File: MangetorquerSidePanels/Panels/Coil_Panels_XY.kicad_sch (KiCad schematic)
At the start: 9 parts, among them J1 Through_Hole_1, J2 MOLEX_2053380006

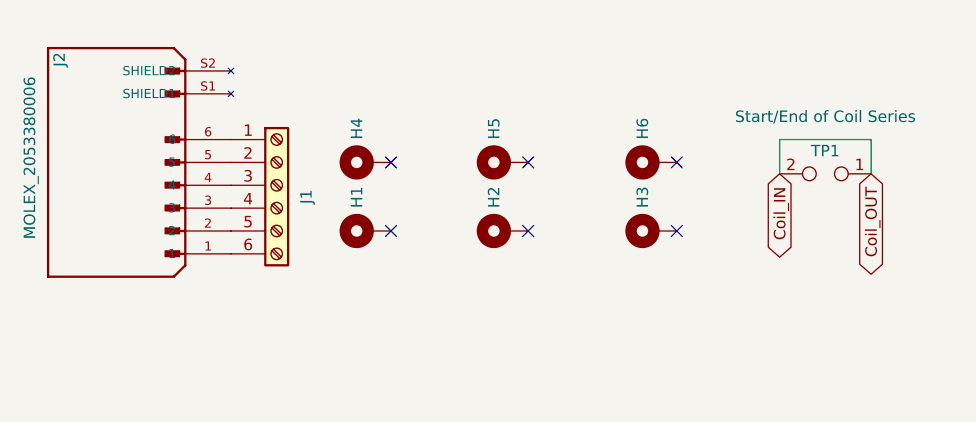
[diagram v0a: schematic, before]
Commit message: Final flight side panels w/ magnetorquers finished, note final board thickness of 0.031'' and updated copper weight of 0.5oz for internal layers
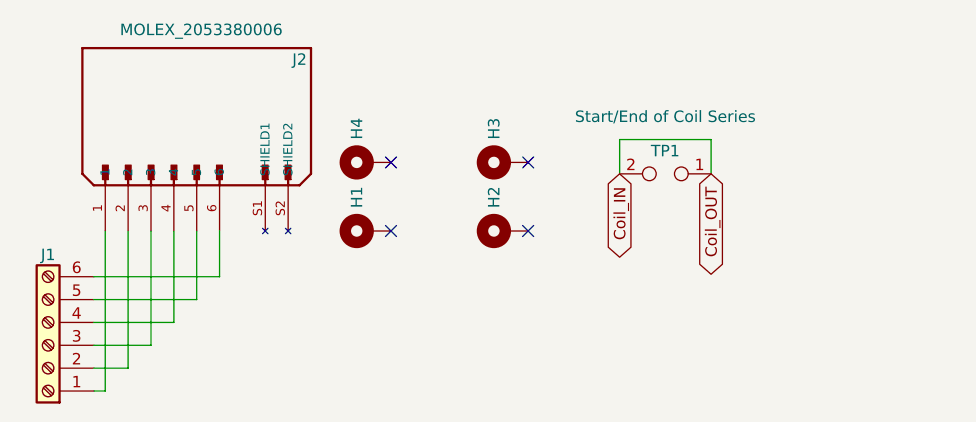
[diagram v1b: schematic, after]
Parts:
- removed H5, H6: ~, MountingHole:MountingHole_2.2mm_M2_DIN965_Pad_TopBottom, symbol Mechanical:MountingHole_Pad
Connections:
- net at J2.1: now also J1.1 (Pin_1); no longer J1.6 (Pin_6)
- net at J2.2: now also J1.2 (Pin_2); no longer J1.5 (Pin_5)
- net at J2.3: now also J1.3 (Pin_3); no longer J1.4 (Pin_4)
- net at J2.4: now also J1.4 (Pin_4); no longer J1.3 (Pin_3)
- net at J2.5: now also J1.5 (Pin_5); no longer J1.2 (Pin_2)
- net at J2.6: now also J1.6 (Pin_6); no longer J1.1 (Pin_1)
- no-connect marks 6 -> 4
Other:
- moved on the sheet: H3, J1, J2, TP1
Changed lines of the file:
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@@
 (kicad_sch (version 20211123) (generator eeschema)
   (paper "A4")
-  (no_connect (at 153.67 92.71))
   (no_connect (at 153.67 100.33))
   (no_connect (at 138.43 92.71))
   (no_connect (at 138.43 100.33))
-  (no_connect (at 170.18 92.71))
-  (no_connect (at 170.18 100.33))
-  (wire (pts (xy 191.77 93.98) (xy 191.77 90.17))
+  (no_connect (at 153.67 92.71))
+  (wire (pts (xy 106.68 118.11) (xy 106.68 100.33))
     (stroke (width 0) (type default) (color 0 0 0 0))
   )
-  (wire (pts (xy 191.77 90.17) (xy 181.61 90.17))
+  (wire (pts (xy 105.41 118.11) (xy 106.68 118.11))
     (stroke (width 0) (type default) (color 0 0 0 0))
   )
-  (wire (pts (xy 181.61 90.17) (xy 181.61 93.98))
+  (wire (pts (xy 105.41 115.57) (xy 109.22 115.57))
     (stroke (width 0) (type default) (color 0 0 0 0))
   )
-  (global_label "Coil_OUT" (shape bidirectional) (at 191.77 93.98 270) (fields_autoplaced)
+  (wire (pts (xy 105.41 107.95) (xy 116.84 107.95))
+    (stroke (width 0) (type default) (color 0 0 0 0))
+  )
+  (wire (pts (xy 116.84 107.95) (xy 116.84 100.33))
+    (stroke (width 0) (type default) (color 0 0 0 0))
+  )
+  (wire (pts (xy 105.41 110.49) (xy 114.3 110.49))
+    (stroke (width 0) (type default) (color 0 0 0 0))
+  )
+  (wire (pts (xy 111.76 113.03) (xy 111.76 100.33))
+    (stroke (width 0) (type default) (color 0 0 0 0))
+  )
+  (wire (pts (xy 109.22 115.57) (xy 109.22 100.33))
+    (stroke (width 0) (type default) (color 0 0 0 0))
+  )
+  (wire (pts (xy 105.41 105.41) (xy 119.38 105.41))
+    (stroke (width 0) (type default) (color 0 0 0 0))
+  )
+  (wire (pts (xy 173.99 93.98) (xy 173.99 90.17))
+    (stroke (width 0) (type default) (color 0 0 0 0))
+  )
+  (wire (pts (xy 114.3 110.49) (xy 114.3 100.33))
+    (stroke (width 0) (type default) (color 0 0 0 0))
+  )
+  (wire (pts (xy 119.38 105.41) (xy 119.38 100.33))
+    (stroke (width 0) (type default) (color 0 0 0 0))
+  )
+  (wire (pts (xy 173.99 90.17) (xy 163.83 90.17))
+    (stroke (width 0) (type default) (color 0 0 0 0))
+  )
+  (wire (pts (xy 163.83 90.17) (xy 163.83 93.98))
+    (stroke (width 0) (type default) (color 0 0 0 0))
+  )
+  (wire (pts (xy 105.41 113.03) (xy 111.76 113.03))
+    (stroke (width 0) (type default) (color 0 0 0 0))
+  )
+  (global_label "Coil_OUT" (shape bidirectional) (at 173.99 93.98 270) (fields_autoplaced)
     (effects (font (size 1.27 1.27)) (justify right))
-    (property "Intersheet References" "${INTERSHEET_REFS}" (id 0) (at 191.8494 104.6783 90)
+    (property "Intersheet References" "${INTERSHEET_REFS}" (id 0) (at 174.0694 104.6783 90)
       (effects (font (size 1.27 1.27)) (justify right) hide)
     )
   )
-  (global_label "Coil_IN" (shape bidirectional) (at 181.61 93.98 270) (fields_autoplaced)
+  (global_label "Coil_IN" (shape bidirectional) (at 163.83 93.98 270) (fields_autoplaced)
     (effects (font (size 1.27 1.27)) (justify right))
-    (property "Intersheet References" "${INTERSHEET_REFS}" (id 0) (at 181.6894 102.985 90)
+    (property "Intersheet References" "${INTERSHEET_REFS}" (id 0) (at 163.9094 102.985 90)
       (effects (font (size 1.27 1.27)) (justify right) hide)
     )
@@
     (pin "1")
   )
-  (symbol (lib_id "solar-panel-side-X-plus-rescue:2053380006-sapling") (at 107.95 92.71 180) (unit 1)
+  (symbol (lib_id "solar-panel-side-X-plus-rescue:2053380006-sapling") (at 116.84 87.63 90) (unit 1)
     (in_bom yes) (on_board yes)
-    (property "Reference" "J2" (id 0) (at 101.6 81.28 90))
-    (property "Value" "MOLEX_2053380006" (id 1) (at 98.298 92.202 90))
-    (property "Footprint" "panels:MOLEX_2053380006" (id 2) (at 107.95 92.71 0)
+    (property "Reference" "J2" (id 0) (at 128.27 81.28 90))
+    (property "Value" "MOLEX_2053380006" (id 1) (at 117.348 77.978 90))
+    (property "Footprint" "panels:MOLEX_2053380006" (id 2) (at 116.84 87.63 0)
       (effects (font (size 1.27 1.27)) hide)
     )
-    (property "Datasheet" "https://www.molex.com/webdocs/datasheets/pdf/en-us/2053380006_PCB_HEADERS.pdf" (id 3) (at 107.95 92.71 0)
+    (property "Datasheet" "https://www.molex.com/webdocs/datasheets/pdf/en-us/2053380006_PCB_HEADERS.pdf" (id 3) (at 116.84 87.63 0)
       (effects (font (size 1.27 1.27)) hide)
     )
@@
     (pin "S2")
   )
-  (symbol (lib_id "Mechanical:MountingHole_Pad") (at 167.64 100.33 90) (unit 1)
-    (in_bom yes) (on_board yes)
-    (property "Reference" "H3" (id 0) (at 166.3954 97.79 0)
-      (effects (font (size 1.27 1.27)) (justify left))
-    )
-    (property "Value" "~" (id 1) (at 168.7068 97.79 0)
-      (effects (font (size 1.27 1.27)) (justify left))
-    )
-    (property "Footprint" "MountingHole:MountingHole_2.2mm_M2_DIN965_Pad_TopBottom" (id 2) (at 167.64 100.33 0)
-      (effects (font (size 1.27 1.27)) hide)
-    )
-    (property "Datasheet" "~" (id 3) (at 167.64 100.33 0)
-      (effects (font (size 1.27 1.27)) hide)
-    )
-    (pin "1")
-  )
-  (symbol (lib_id "Connector:Screw_Terminal_01x06") (at 125.73 95.25 0) (unit 1)
-    (in_bom yes) (on_board yes) (fields_autoplaced)
-    (property "Reference" "J1" (id 0) (at 129.0304 96.52 90))
-    (property "Value" "Through_Hole_1" (id 1) (at 131.5673 96.52 90)
-      (effects (font (size 1.27 1.27)) hide)
-    )
-    (property "Footprint" "Connector_PinHeader_2.54mm:PinHeader_1x06_P2.54mm_Vertical" (id 2) (at 125.73 95.25 0)
-      (effects (font (size 1.27 1.27)) hide)
-    )
-    (property "Datasheet" "~" (id 3) (at 125.73 95.25 0)
-      (effects (font (size 1.27 1.27)) hide)
-    )
-    (pin "1")
-    (pin "2")
-    (pin "3")
-    (pin "4")
-    (pin "5")
-    (pin "6")
-  )
-  (symbol (lib_id "Mechanical:MountingHole_Pad") (at 167.64 92.71 90) (unit 1)
-    (in_bom yes) (on_board yes)
-    (property "Reference" "H6" (id 0) (at 166.3954 90.17 0)
-      (effects (font (size 1.27 1.27)) (justify left))
-    )
-    (property "Value" "~" (id 1) (at 168.7068 90.17 0)
-      (effects (font (size 1.27 1.27)) (justify left))
-    )
-    (property "Footprint" "MountingHole:MountingHole_2.2mm_M2_DIN965_Pad_TopBottom" (id 2) (at 167.64 92.71 0)
-      (effects (font (size 1.27 1.27)) hide)
-    )
-    (property "Datasheet" "~" (id 3) (at 167.64 92.71 0)
-      (effects (font (size 1.27 1.27)) hide)
-    )
-    (pin "1")
-  )
   (symbol (lib_id "Mechanical:MountingHole_Pad") (at 151.13 92.71 90) (unit 1)
     (in_bom yes) (on_board yes)
-    (property "Reference" "H5" (id 0) (at 149.8854 90.17 0)
+    (property "Reference" "H3" (id 0) (at 149.8854 90.17 0)
       (effects (font (size 1.27 1.27)) (justify left))
     )
@@
     (pin "1")
   )
-  (symbol (lib_id "Connector:TestPoint_2Pole") (at 186.69 93.98 180) (unit 1)
-    (in_bom yes) (on_board yes)
-    (property "Reference" "TP1" (id 0) (at 186.69 91.44 0))
-    (property "Value" "Start/End of Coil Series" (id 1) (at 186.69 87.63 0))
-    (property "Footprint" "panels:TestPointConnection" (id 2) (at 186.69 93.98 0)
+  (symbol (lib_id "Connector:Screw_Terminal_01x06") (at 100.33 113.03 180) (unit 1)
+    (in_bom yes) (on_board yes) (fields_autoplaced)
+    (property "Reference" "J1" (id 0) (at 100.33 102.9772 0))
+    (property "Value" "Through_Hole_1" (id 1) (at 94.4927 111.76 90)
       (effects (font (size 1.27 1.27)) hide)
     )
-    (property "Datasheet" "~" (id 3) (at 186.69 93.98 0)
+    (property "Footprint" "Connector_PinHeader_2.54mm:PinHeader_1x06_P2.54mm_Vertical" (id 2) (at 100.33 113.03 0)
+      (effects (font (size 1.27 1.27)) hide)
+    )
+    (property "Datasheet" "~" (id 3) (at 100.33 113.03 0)
+      (effects (font (size 1.27 1.27)) hide)
+    )
+    (pin "1")
+    (pin "2")
+    (pin "3")
+    (pin "4")
+    (pin "5")
+    (pin "6")
+  )
+  (symbol (lib_id "Connector:TestPoint_2Pole") (at 168.91 93.98 180) (unit 1)
+    (in_bom yes) (on_board yes)
+    (property "Reference" "TP1" (id 0) (at 168.91 91.44 0))
+    (property "Value" "Start/End of Coil Series" (id 1) (at 168.91 87.63 0))
+    (property "Footprint" "panels:TestPointConnection" (id 2) (at 168.91 93.98 0)
+      (effects (font (size 1.27 1.27)) hide)
+    )
+    (property "Datasheet" "~" (id 3) (at 168.91 93.98 0)
       (effects (font (size 1.27 1.27)) hide)
     )
@@
       (reference "H4") (unit 1) (value "~") (footprint "MountingHole:MountingHole_2.2mm_M2_DIN965_Pad_TopBottom")
     )
-    (path "/ceea3dc6-0906-4028-9990-6c6bfea00ca3"
-      (reference "H5") (unit 1) (value "~") (footprint "MountingHole:MountingHole_2.2mm_M2_DIN965_Pad_TopBottom")
-    )
-    (path "/c9168a08-b435-4b88-8dd0-a8a31a8fc32b"
-      (reference "H6") (unit 1) (value "~") (footprint "MountingHole:MountingHole_2.2mm_M2_DIN965_Pad_TopBottom")
-    )
     (path "/c6112166-6cb8-4cf8-90b5-cb35aeda56bf"
